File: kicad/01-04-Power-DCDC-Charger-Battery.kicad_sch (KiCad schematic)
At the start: 38 parts, among them J3 S2B-PH-K-S_LF__SN_, Q1 PMOS, Q2 AO3400A, Q3 AO3400A, U4 MCP73831-2-OT, U5 BQ29700DSER, U6 TLV62568DBV

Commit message: working on dcdc
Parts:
- added D5: 1N4148WT, Diode_SMD:D_SOD-523, symbol Diode:1N4148WT
- added D6: BAT43, Diode_THT:D_DO-35_SOD27_P7.62mm_Horizontal, symbol Diode:BAT43
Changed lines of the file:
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@@
+	)
+	(symbol
+		(lib_id "Diode:BAT43")
+		(at 172.72 132.08 270)
+		(unit 1)
+		(exclude_from_sim no)
+		(in_bom yes)
+		(on_board yes)
+		(dnp no)
+		(fields_autoplaced yes)
+		(property "Reference" "D6"
+			(at 175.26 130.4924 90)
+			(effects
+				(font
+					(size 1.27 1.27)
+				)
+				(justify left)
+			)
+		)
+		(property "Value" "BAT43"
+			(at 175.26 133.0324 90)
+			(effects
+				(font
+					(size 1.27 1.27)
+				)
+				(justify left)
+			)
+		)
+		(property "Footprint" "Diode_THT:D_DO-35_SOD27_P7.62mm_Horizontal"
+			(at 168.275 132.08 0)
+			(effects
+				(font
+					(size 1.27 1.27)
+				)
+				(hide yes)
+			)
+		)
+		(property "Datasheet" "http://www.vishay.com/docs/85660/bat42.pdf"
+			(at 172.72 132.08 0)
+			(effects
+				(font
+					(size 1.27 1.27)
+				)
+				(hide yes)
+			)
+		)
+		(property "Description" "30V 0.2A Small Signal Schottky Diode, DO-35"
+			(at 172.72 132.08 0)
+			(effects
+				(font
+					(size 1.27 1.27)
+				)
+				(hide yes)
+			)
+		)
+		(pin "1"
+		)
+		(pin "2"
+		)
+		(instances
+			(project ""
+				(path "/9d26b66f-2a94-42e5-8460-016e0bf95186/9c84c2c8-9981-4486-adaf-4a40ca17b6d0"
+					(reference "D6")
+					(unit 1)
+				)
+			)
+		)
 	)
 	(symbol
@@
 					(unit 1)
 				)
+			)
+		)
+	)
+	(symbol
+		(lib_id "Diode:1N4148WT")
+		(at 151.13 132.08 270)
+		(unit 1)
+		(exclude_from_sim no)
+		(in_bom yes)
+		(on_board yes)
+		(dnp no)
+		(fields_autoplaced yes)
+		(property "Reference" "D5"
+			(at 153.67 130.8099 90)
+			(effects
+				(font
+					(size 1.27 1.27)
+				)
+				(justify left)
+			)
+		)
+		(property "Value" "1N4148WT"
+			(at 153.67 133.3499 90)
+			(effects
+				(font
+					(size 1.27 1.27)
+				)
+				(justify left)
+			)
+		)
+		(property "Footprint" "Diode_SMD:D_SOD-523"
+			(at 146.685 132.08 0)
+			(effects
+				(font
+					(size 1.27 1.27)
+				)
+				(hide yes)
+			)
+		)
+		(property "Datasheet" "https://www.diodes.com/assets/Datasheets/ds30396.pdf"
+			(at 151.13 132.08 0)
+			(effects
+				(font
+					(size 1.27 1.27)
+				)
+				(hide yes)
+			)
+		)
+		(property "Description" "75V 0.15A Fast switching Diode, SOD-523"
+			(at 151.13 132.08 0)
+			(effects
+				(font
+					(size 1.27 1.27)
+				)
+				(hide yes)
+			)
+		)
+		(property "Sim.Device" "D"
+			(at 151.13 132.08 0)
+			(effects
+				(font
+					(size 1.27 1.27)
+				)
+				(hide yes)
+			)
+		)
+		(property "Sim.Pins" "1=K 2=A"
+			(at 151.13 132.08 0)
+			(effects
+				(font
+					(size 1.27 1.27)
+				)
+				(hide yes)
+			)
+		)
+		(pin "2"
+		)
+		(pin "1"
+		)
+		(instances
+			(project ""
+				(path "/9d26b66f-2a94-42e5-8460-016e0bf95186/9c84c2c8-9981-4486-adaf-4a40ca17b6d0"
+					(reference "D5")
+					(unit 1)
+				)

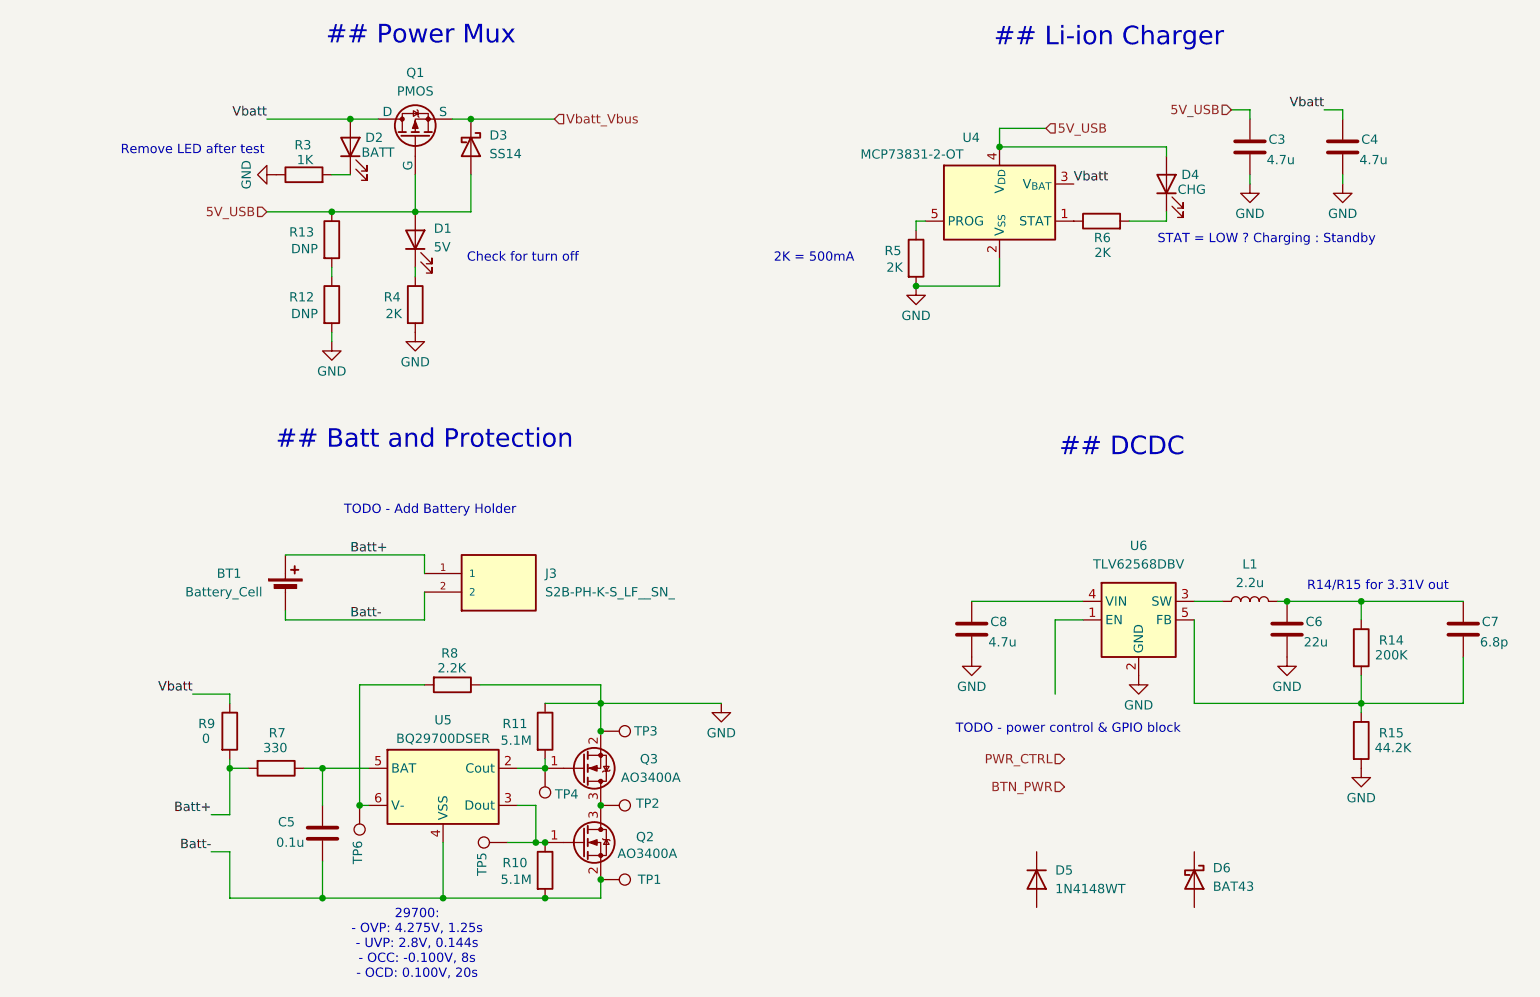
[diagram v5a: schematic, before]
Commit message: dcdc enable and swd
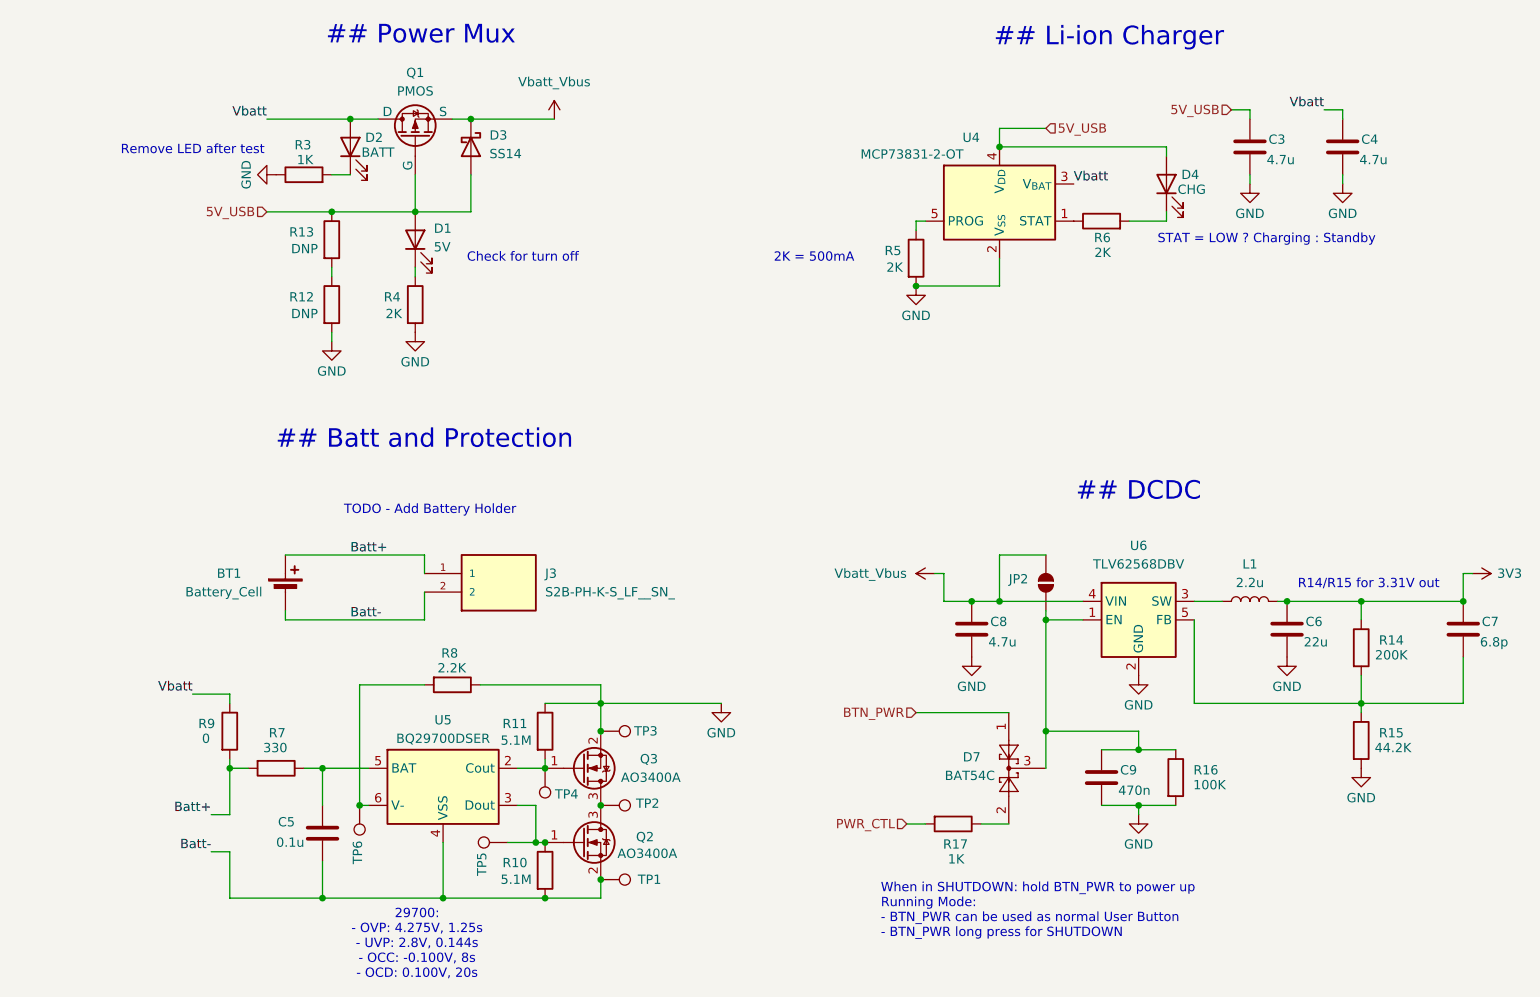
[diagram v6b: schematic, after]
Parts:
- removed D5: 1N4148WT, Diode_SMD:D_SOD-523, symbol Diode:1N4148WT
- removed D6: BAT43, Diode_THT:D_DO-35_SOD27_P7.62mm_Horizontal, symbol Diode:BAT43
- added C9: 470n, symbol Device:C
- added D7: BAT54C, Package_TO_SOT_SMD:SOT-23, symbol Diode:BAT54C
- added JP2: SolderJumper_2_Open, symbol Jumper:SolderJumper_2_Open
- added R16: 100K, symbol Device:R
- added R17: 1K, symbol Device:R
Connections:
- net BTN_PWR: now also D7.1
- net GND: now also C9.2, R16.2
- net Vbatt_Vbus: now also C8.1, U6.4 (VIN), JP2.2 (B)
- net 3V3: now reaches C6.1, C7.1, L1.2, R14.1
- net at U6.1 (EN): now also C9.1, D7.3, JP2.1 (A), R16.1
- new net: D7.2, R17.1
- new net PWR_CTL: R17.2
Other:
- note added: "When in SHUTDOWN: hold BTN_PWR to power up Running Mode: - BTN_PWR can be used as normal User Button - BTN_PWR long press for SHUTDOWN"
- note removed: "TODO - power control & GPIO block"

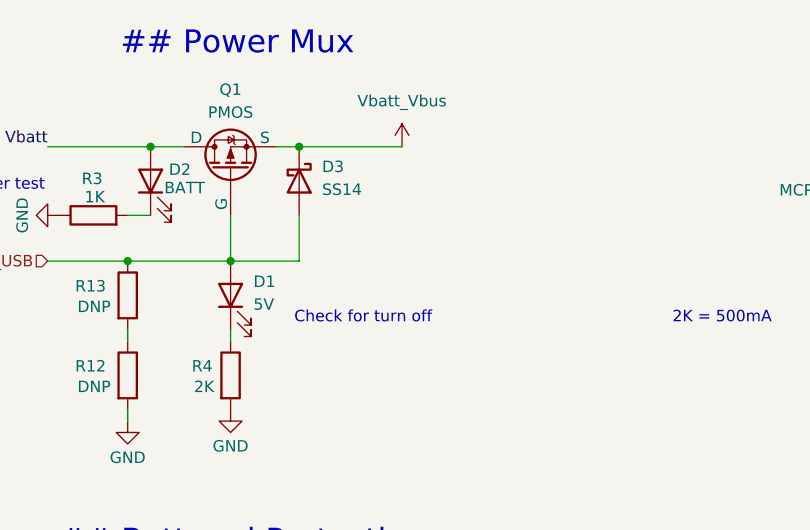
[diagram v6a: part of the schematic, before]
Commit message: rp2040 chip start
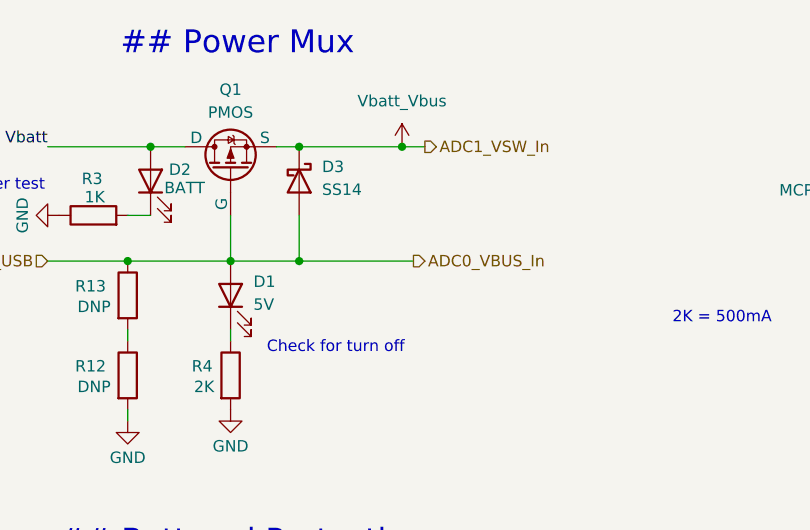
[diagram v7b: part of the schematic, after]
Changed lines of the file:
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@@
 	(text "Check for turn off"
 		(exclude_from_sim no)
-		(at 80.772 46.99 0)
+		(at 77.724 50.292 0)
 		(effects
 			(font
@@
 	)
 	(junction
+		(at 73.66 40.64)
+		(diameter 0)
+		(color 0 0 0 0)
+	)
+	(junction
 		(at 152.4 96.52)
 		(diameter 0)
@@
 	)
 	(junction
+		(at 85.09 27.94)
+		(diameter 0)
+		(color 0 0 0 0)
+	)
+	(junction
 		(at 142.24 93.98)
 		(diameter 0)
@@
 	(wire
 		(pts
+			(xy 85.09 27.94) (xy 87.63 27.94)
+		)
+		(stroke
+			(width 0)
+			(type default)
+		)
+	)
+	(wire
+		(pts
 			(xy 40.64 128.27) (xy 40.64 134.62)
 		)
@@
 		(pts
 			(xy 168.91 40.64) (xy 168.91 41.91)
+		)
+		(stroke
+			(width 0)
+			(type default)
+		)
+	)
+	(wire
+		(pts
+			(xy 73.66 40.64) (xy 86.36 40.64)
 		)
 		(stroke
@@
 		)
 	)
+	(hierarchical_label "ADC0_VBUS_In"
+		(shape output)
+		(at 86.36 40.64 0)
+		(effects
+			(font
+				(size 1.27 1.27)
+			)
+			(justify left)
+		)
+	)
 	(hierarchical_label "5V_USB"
 		(shape input)
@@
 		)
 	)
+	(hierarchical_label "ADC1_VSW_In"
+		(shape output)
+		(at 87.63 27.94 0)
+		(effects
+			(font
+				(size 1.27 1.27)
+			)
+			(justify left)
+		)
+	)

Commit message: mcu periphs
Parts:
- renumbered C5 to C3, C8 to C4, C9 to C5, C3 to C6, C6 to C7, C4 to C8, C7 to C9, D2 to D1, D1 to D2, D7 to D4, D4 to D5, Q3 to Q2, Q2 to Q3, R11 to R10, R10 to R11, R5 to R12, R17 to R13, R6 to R14, R16 to R15, R14 to R16, R15 to R17, R9 to R3, R7 to R4, R3 to R5, R13 to R6, R12 to R7, R4 to R8, R8 to R9, TP6 to TP1, TP5 to TP2, TP4 to TP3, TP3 to TP4, TP2 to TP5, TP1 to TP6, U5 to U2, U4 to U3, U6 to U4
